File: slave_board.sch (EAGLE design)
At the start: 157 parts, among them IC3 ATMEGA2560-16AU, J1 OSTVN08A150, J11 1935161, J12 OSTVN06A150, J13 OSTVN08A150, J17 RJ45, J18 OSTVN08A150, J2 OSTVN08A150, J22 RJ45, J3 1935161, J4 OSTVN06A150, J6 1935161, J8 OSTVN08A150, K1 ORWH-SH-112D1F, Q1 PHB45NQ15T, Q2 PHB45NQ15T, Q3 BSS138L, Q5 BSS138L, Q7 PHB45NQ15T, Q8 IRFR9024TRPBF, U1 VNQ5E160KTR-E, U2 PCA9615, U3 INA213AIDCKT, U4 VNH7070ASTR, U5 VNH7070ASTR, U6 VNQ5E160KTR-E, U7 INA213AIDCKT, U8 LM340MP-5.0/NOPB, U9 LM340MP-5.0/NOPB, Y1 ABLS-16.000MHZ-B4-T

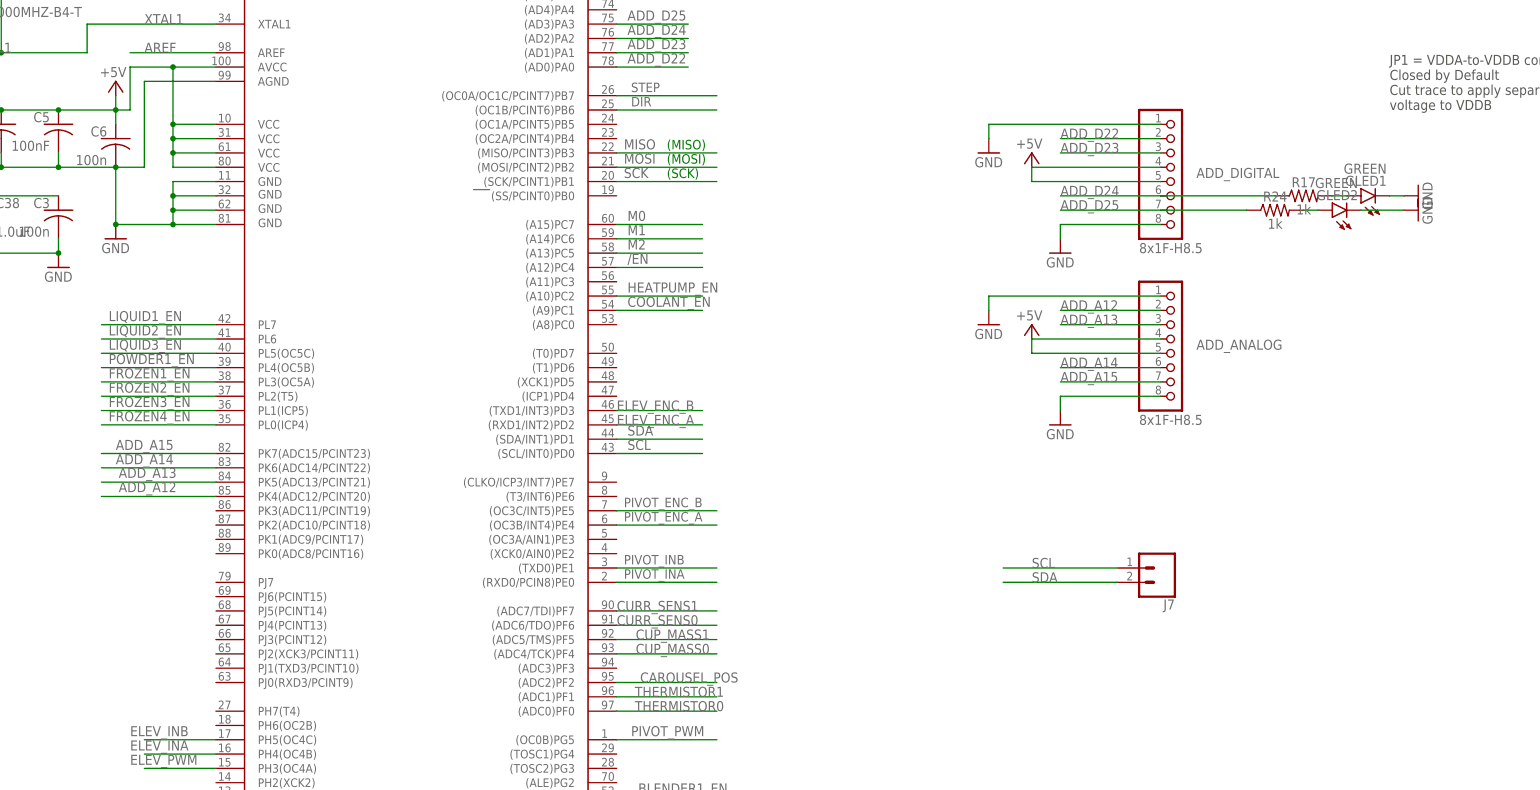
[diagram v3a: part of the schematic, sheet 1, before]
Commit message: Moved uc pins; fixed all DRCs
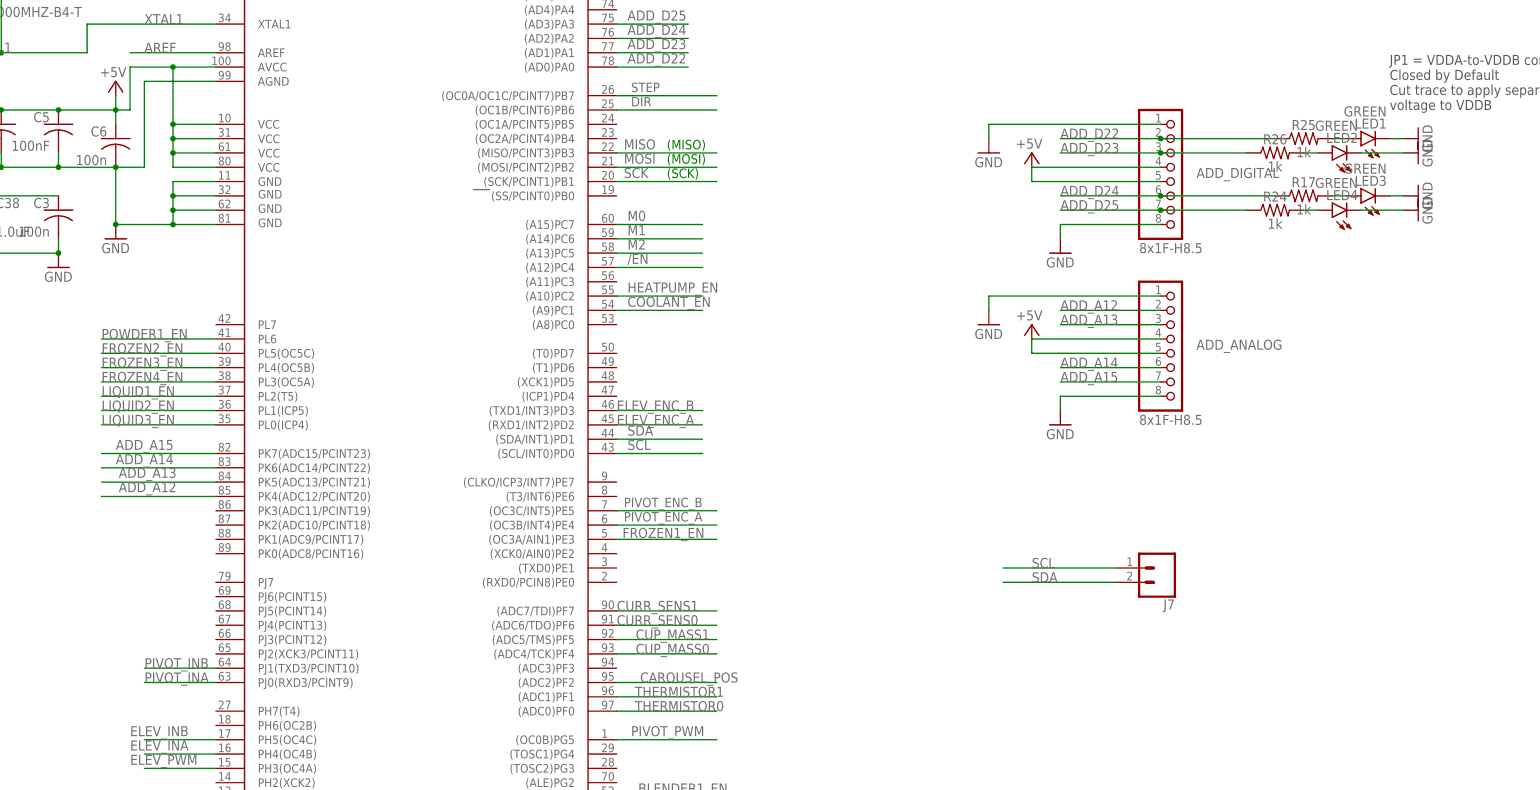
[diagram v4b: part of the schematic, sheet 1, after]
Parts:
- added LED1, LED2: GREEN, led:LEDCHIP-LED0805
- added R25, R26: 1k, SparkFun-Resistors:1KOHM-0603-1/10W-1%
- renumbered GLED1 to LED3, GLED2 to LED4
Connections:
- new net N$10: LED2.A, R26.2
- new net N$9: LED1.A, R25.2
- net ADD_D22: now also R25.1
- net ADD_D23: now also R26.1
- net FROZEN1_EN: now also IC3.(OC3A/AIN1)PE3; no longer IC3.PL3(OC5A)
- net FROZEN2_EN: now also IC3.PL5(OC5C); no longer IC3.PL2(T5)
- net FROZEN3_EN: now also IC3.PL4(OC5B); no longer IC3.PL1(ICP5)
- net FROZEN4_EN: now also IC3.PL3(OC5A); no longer IC3.PL0(ICP4)
- net GND: now also LED1.C, LED2.C
- net LIQUID1_EN: now also IC3.PL2(T5); no longer IC3.PL7
- net LIQUID2_EN: now also IC3.PL1(ICP5); no longer IC3.PL6
- net LIQUID3_EN: now also IC3.PL0(ICP4); no longer IC3.PL5(OC5C)
- net PIVOT_INA: now also IC3.PJ0(RXD3/PCINT9); no longer IC3.(RXD0/PCIN8)PE0
- net PIVOT_INB: now also IC3.PJ1(TXD3/PCINT10); no longer IC3.(TXD0)PE1
- net POWDER1_EN: now also IC3.PL6; no longer IC3.PL4(OC5B)

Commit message: broke blender enable to terminal blocks
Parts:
- added J14, J15: (no value), SparkFun-Connectors:CONN_02
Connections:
- net BLENDER0_EN: now also J14.1
- net BLENDER1_EN: now also J14.2
- net CURR_SENS0: now also J15.1
- net CURR_SENS1: now also J15.2
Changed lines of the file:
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@@
 <part name="GND80" library="supply1" library_urn="urn:adsk.eagle:library:371" deviceset="GND" device=""/>
 <part name="R26" library="SparkFun-Resistors" library_urn="urn:adsk.eagle:library:532" deviceset="1KOHM" device="-0603-1/10W-1%" package3d_urn="urn:adsk.eagle:package:39650/1" value="1k"/>
+<part name="J14" library="SparkFun-Connectors" library_urn="urn:adsk.eagle:library:513" deviceset="CONN_02" device="" package3d_urn="urn:adsk.eagle:package:38039/1"/>
+<part name="J15" library="SparkFun-Connectors" library_urn="urn:adsk.eagle:library:513" deviceset="CONN_02" device="" package3d_urn="urn:adsk.eagle:package:38039/1"/>
 </parts>
 <sheets>
@@
 <attribute name="NAME" x="322.58" y="156.464" size="1.778" layer="95" font="vector" align="bottom-center"/>
 <attribute name="VALUE" x="322.58" y="153.416" size="1.778" layer="96" font="vector" align="top-center"/>
+</instance>
+<instance part="J14" gate="G$1" x="302.26" y="60.96" smashed="yes" rot="R180">
+<attribute name="VALUE" x="304.8" y="65.786" size="1.778" layer="96" font="vector" rot="R180"/>
+<attribute name="NAME" x="304.8" y="55.372" size="1.778" layer="95" font="vector" rot="R180"/>
+</instance>
+<instance part="J15" gate="G$1" x="302.26" y="43.18" smashed="yes" rot="R180">
+<attribute name="VALUE" x="304.8" y="48.006" size="1.778" layer="96" font="vector" rot="R180"/>
+<attribute name="NAME" x="304.8" y="37.592" size="1.778" layer="95" font="vector" rot="R180"/>
 </instance>
 </instances>
@@
 <pinref part="IC3" gate="1" pin="(WR)PG0"/>
 </segment>
+<segment>
+<pinref part="J14" gate="G$1" pin="1"/>
+<wire x1="294.64" y1="60.96" x2="274.32" y2="60.96" width="0.1524" layer="91"/>
+<label x="274.32" y="60.96" size="1.778" layer="95"/>
+</segment>
 </net>
 <net name="BLENDER1_EN" class="0">
@@
 <label x="209.55" y="41.275" size="1.778" layer="95"/>
 <pinref part="IC3" gate="1" pin="(RD)PG1"/>
+</segment>
+<segment>
+<pinref part="J14" gate="G$1" pin="2"/>
+<wire x1="294.64" y1="58.42" x2="274.32" y2="58.42" width="0.1524" layer="91"/>
+<label x="274.32" y="58.42" size="1.778" layer="95"/>
 </segment>
 </net>
@@
 <label x="205.74" y="71.12" size="1.778" layer="95"/>
 </segment>
+<segment>
+<pinref part="J15" gate="G$1" pin="1"/>
+<wire x1="294.64" y1="43.18" x2="274.32" y2="43.18" width="0.1524" layer="91"/>
+<label x="276.86" y="43.18" size="1.778" layer="95"/>
+</segment>
 </net>
 <net name="CURR_SENS1" class="0">
@@
 <label x="205.74" y="73.66" size="1.778" layer="95"/>
 </segment>
-</net>
+<segment>
+<pinref part="J15" gate="G$1" pin="2"/>
+<wire x1="294.64" y1="40.64" x2="274.32" y2="40.64" width="0.1524" layer="91"/>
+<label x="276.86" y="40.64" size="1.778" layer="95"/>
+</segment>
+</net>

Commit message: Morning changes from board review
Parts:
- removed J12: OSTVN06A150, smoothio:OSTVN06A150
- added J16: OSTVN08A150, smoothio:OSTVN08A150
- added L1: 742792651, smoothio:742792651
- added R27, R28, R29, R30: 10k, SparkFun-Resistors:10KOHM-0603-1/10W-1%
- J1, J2: value OSTVN08A150 -> OSTVN06A150; device smoothio:OSTVN08A150 -> smoothio:OSTVN06A150
- J5: value (none) -> OSTVN06A150; device SparkFun-Connectors:CONN_05 -> smoothio:OSTVN06A150
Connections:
- removed net CUP_SENSE0: IC3.(AD6)PA6, J4.5
- removed net CUP_SENSE1: IC3.(AD7)PA7, J12.5
- new net GND2: C19.-, C20.-, C21.-, D3.A, D5.A, L1.1, R1.1, R14.1, U3.IN-, U7.IN-
- new net LIMIT_SENSE: IC3.(ALE)PG2, J1.1, R28.2
- net +5V: now also J1.3, J1.6, J16.5, J16.8, R27.1, R28.1, R29.1, R30.1; no longer J1.8, J12.3, J12.6, J2.5
- net A1: now also J5.3; no longer J5.2
- net A2: now also J5.2; no longer J5.1
- net B1: now also J5.4; no longer J5.3
- net B2: now also J5.5; no longer J5.4
- net CAROUSEL_POS: now also J1.4, R27.2; no longer J1.6
- net CUP_MASS1: now also J4.5; no longer J12.2
- net ELEV_ENC_A: now also J16.6, R29.2; no longer J2.8
- net ELEV_ENC_B: now also J16.3, R30.2; no longer J2.7
- net GND: now also J1.2, J16.1, J16.4, J16.7, L1.2; no longer C19.-, C20.-, C21.-, D3.A, D5.A, J1.1, J1.3, J1.7, J12.1, J12.4, R1.1, R14.1, U3.IN-, U7.IN-
- net THERMISTOR0: now also J2.5; no longer J1.2
- net THERMISTOR1: now also J16.2; no longer J1.4
- net V-STEPPER: now also J5.6; no longer J5.5
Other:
- note added: "Ferrite bead 742792651"

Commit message: Finished review changes
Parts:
- removed R27: 10k, SparkFun-Resistors:10KOHM-0603-1/10W-1%
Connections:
- net +5V: no longer R27.1
- net CAROUSEL_POS: no longer R27.2
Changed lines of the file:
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@@
 <part name="J2" library="smoothio" deviceset="OSTVN06A150" device=""/>
 <part name="J5" library="smoothio" deviceset="OSTVN06A150" device=""/>
-<part name="R27" library="SparkFun-Resistors" library_urn="urn:adsk.eagle:library:532" deviceset="10KOHM" device="-0603-1/10W-1%" package3d_urn="urn:adsk.eagle:package:39650/1" value="10k"/>
 <part name="R28" library="SparkFun-Resistors" library_urn="urn:adsk.eagle:library:532" deviceset="10KOHM" device="-0603-1/10W-1%" package3d_urn="urn:adsk.eagle:package:39650/1" value="10k"/>
 <part name="R29" library="SparkFun-Resistors" library_urn="urn:adsk.eagle:library:532" deviceset="10KOHM" device="-0603-1/10W-1%" package3d_urn="urn:adsk.eagle:package:39650/1" value="10k"/>
@@
 </segment>
 </net>
-<net name="GND" class="2">
+<net name="GND" class="0">
 <segment>
 <wire x1="248.92" y1="210.82" x2="246.38" y2="210.82" width="0.1524" layer="91"/>
@@
 </segment>
 </net>
-<net name="GND" class="2">
+<net name="GND" class="0">
 <segment>
 <wire x1="76.2" y1="172.72" x2="63.5" y2="172.72" width="0.1524" layer="91"/>
@@
 </segment>
 </net>
-<net name="GND" class="2">
+<net name="GND" class="0">
 <segment>
 <pinref part="U1" gate="G$1" pin="GND"/>
@@
 </busses>
 <nets>
-<net name="GND" class="2">
+<net name="GND" class="0">
 <segment>
 <pinref part="C23" gate="G$1" pin="-"/>
@@
 <attribute name="NAME" x="50.8" y="69.088" size="1.778" layer="95" font="vector"/>
 </instance>
-<instance part="R27" gate="G$1" x="86.36" y="106.68" smashed="yes" rot="R180">
-<attribute name="NAME" x="86.36" y="105.156" size="1.778" layer="95" font="vector" rot="R180" align="bottom-center"/>
-<attribute name="VALUE" x="86.36" y="108.204" size="1.778" layer="96" font="vector" rot="R180" align="top-center"/>
-</instance>
 <instance part="R28" gate="G$1" x="86.36" y="99.06" smashed="yes" rot="R180">
 <attribute name="NAME" x="86.36" y="97.536" size="1.778" layer="95" font="vector" rot="R180" align="bottom-center"/>
@@
 <pinref part="P+9" gate="1" pin="+5V"/>
 <wire x1="93.98" y1="114.3" x2="93.98" y2="111.76" width="0.1524" layer="91"/>
-<pinref part="R27" gate="G$1" pin="1"/>
-<wire x1="91.44" y1="106.68" x2="93.98" y2="106.68" width="0.1524" layer="91"/>
-<wire x1="93.98" y1="106.68" x2="93.98" y2="111.76" width="0.1524" layer="91"/>
+<wire x1="93.98" y1="104.14" x2="93.98" y2="111.76" width="0.1524" layer="91"/>
 <junction x="93.98" y="111.76"/>
 <wire x1="60.96" y1="104.14" x2="93.98" y2="104.14" width="0.1524" layer="91"/>
-<wire x1="93.98" y1="104.14" x2="93.98" y2="106.68" width="0.1524" layer="91"/>
-<junction x="93.98" y="106.68"/>
 <pinref part="R28" gate="G$1" pin="1"/>
 <wire x1="91.44" y1="99.06" x2="93.98" y2="99.06" width="0.1524" layer="91"/>
@@
 </segment>
 </net>
-<net name="GND" class="2">
+<net name="GND" class="0">
 <segment>
 <wire x1="50.8" y1="154.94" x2="55.88" y2="154.94" width="0.1524" layer="91"/>
@@
 <wire x1="60.96" y1="106.68" x2="81.28" y2="106.68" width="0.1524" layer="91"/>
 <label x="60.96" y="106.68" size="1.778" layer="95"/>
-<pinref part="R27" gate="G$1" pin="2"/>
 <pinref part="J1" gate="G$1" pin="4"/>
 </segment>
@@
 </segment>
 </net>
-<net name="GND" class="2">
+<net name="GND" class="0">
 <segment>
 <wire x1="218.44" y1="134.62" x2="236.22" y2="134.62" width="0.1524" layer="91"/>

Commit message: Few more changes
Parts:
- added J12: (no value), SparkFun-Connectors:CONN_02
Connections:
- net BLENDER0_EN: now also J12.1; no longer J14.1
- net BLENDER0_GATE: now also J14.1
- net BLENDER1_EN: now also J12.2; no longer J14.2
- net BLENDER1_GATE: now also J14.2
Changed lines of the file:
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@@
 <part name="GND80" library="supply1" library_urn="urn:adsk.eagle:library:371" deviceset="GND" device=""/>
 <part name="R26" library="SparkFun-Resistors" library_urn="urn:adsk.eagle:library:532" deviceset="1KOHM" device="-0603-1/10W-1%" package3d_urn="urn:adsk.eagle:package:39650/1" value="1k"/>
-<part name="J14" library="SparkFun-Connectors" library_urn="urn:adsk.eagle:library:513" deviceset="CONN_02" device="" package3d_urn="urn:adsk.eagle:package:38039/1"/>
 <part name="J15" library="SparkFun-Connectors" library_urn="urn:adsk.eagle:library:513" deviceset="CONN_02" device="" package3d_urn="urn:adsk.eagle:package:38039/1"/>
 <part name="J16" library="smoothio" deviceset="OSTVN08A150" device=""/>
@@
 <part name="SUPPLY4" library="supply2" library_urn="urn:adsk.eagle:library:372" deviceset="GND2" device=""/>
 <part name="SUPPLY5" library="supply2" library_urn="urn:adsk.eagle:library:372" deviceset="GND2" device=""/>
+<part name="J12" library="SparkFun-Connectors" library_urn="urn:adsk.eagle:library:513" deviceset="CONN_02" device="" package3d_urn="urn:adsk.eagle:package:38039/1"/>
+<part name="J14" library="SparkFun-Connectors" library_urn="urn:adsk.eagle:library:513" deviceset="CONN_02" device="" package3d_urn="urn:adsk.eagle:package:38039/1"/>
 </parts>
 <sheets>
@@
 <attribute name="NAME" x="322.58" y="156.464" size="1.778" layer="95" font="vector" align="bottom-center"/>
 <attribute name="VALUE" x="322.58" y="153.416" size="1.778" layer="96" font="vector" align="top-center"/>
-</instance>
-<instance part="J14" gate="G$1" x="302.26" y="60.96" smashed="yes" rot="R180">
-<attribute name="VALUE" x="304.8" y="65.786" size="1.778" layer="96" font="vector" rot="R180"/>
-<attribute name="NAME" x="304.8" y="55.372" size="1.778" layer="95" font="vector" rot="R180"/>
 </instance>
 <instance part="J15" gate="G$1" x="302.26" y="43.18" smashed="yes" rot="R180">
@@
 <pinref part="IC3" gate="1" pin="(WR)PG0"/>
 </segment>
-<segment>
-<pinref part="J14" gate="G$1" pin="1"/>
-<wire x1="294.64" y1="60.96" x2="274.32" y2="60.96" width="0.1524" layer="91"/>
-<label x="274.32" y="60.96" size="1.778" layer="95"/>
-</segment>
 </net>
 <net name="BLENDER1_EN" class="0">
@@
 <label x="209.55" y="41.275" size="1.778" layer="95"/>
 <pinref part="IC3" gate="1" pin="(RD)PG1"/>
-</segment>
-<segment>
-<pinref part="J14" gate="G$1" pin="2"/>
-<wire x1="294.64" y1="58.42" x2="274.32" y2="58.42" width="0.1524" layer="91"/>
-<label x="274.32" y="58.42" size="1.778" layer="95"/>
 </segment>
 </net>
@@
 <attribute name="NAME" x="340.36" y="185.928" size="1.778" layer="95" font="vector"/>
 </instance>
+<instance part="J12" gate="G$1" x="363.22" y="116.84" smashed="yes" rot="R180">
+<attribute name="VALUE" x="365.76" y="121.666" size="1.778" layer="96" font="vector" rot="R180"/>
+<attribute name="NAME" x="365.76" y="111.252" size="1.778" layer="95" font="vector" rot="R180"/>
+</instance>
+<instance part="J14" gate="G$1" x="363.22" y="96.52" smashed="yes" rot="R180">
+<attribute name="VALUE" x="365.76" y="101.346" size="1.778" layer="96" font="vector" rot="R180"/>
+<attribute name="NAME" x="365.76" y="90.932" size="1.778" layer="95" font="vector" rot="R180"/>
+</instance>
 </instances>
 <busses>
@@
 <pinref part="EL3H7-2" gate="G$1" pin="1"/>
 </segment>
+<segment>
+<pinref part="J12" gate="G$1" pin="2"/>
+<wire x1="355.6" y1="114.3" x2="335.28" y2="114.3" width="0.1524" layer="91"/>
+<label x="335.28" y="114.3" size="1.778" layer="95"/>
+</segment>
 </net>
 <net name="COOLANT_EN" class="0">
@@
 <pinref part="EL3H7-1" gate="G$1" pin="1"/>
 </segment>
+<segment>
+<pinref part="J12" gate="G$1" pin="1"/>
+<wire x1="355.6" y1="116.84" x2="335.28" y2="116.84" width="0.1524" layer="91"/>
+<label x="335.28" y="116.84" size="1.778" layer="95"/>
+</segment>
 </net>
 <net name="V-HEATPUMP" class="3">
@@
 <label x="259.08" y="68.58" size="1.778" layer="95"/>
 </segment>
+<segment>
+<pinref part="J14" gate="G$1" pin="2"/>
+<wire x1="355.6" y1="93.98" x2="335.28" y2="93.98" width="0.1524" layer="91"/>
+<label x="335.28" y="93.98" size="1.778" layer="95"/>
+</segment>
 </net>
 <net name="N$14" class="0">
@@
 <label x="259.08" y="104.14" size="1.778" layer="95"/>
 </segment>
-</net>
+<segment>
+<pinref part="J14" gate="G$1" pin="1"/>
+<wire x1="355.6" y1="96.52" x2="335.28" y2="96.52" width="0.1524" layer="91"/>
+<label x="335.28" y="96.52" size="1.778" layer="95"/>
+</segment>
+</net>
